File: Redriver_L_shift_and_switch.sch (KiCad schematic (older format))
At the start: 12 parts, among them U3 SN74AVCH16T245_DGV_48

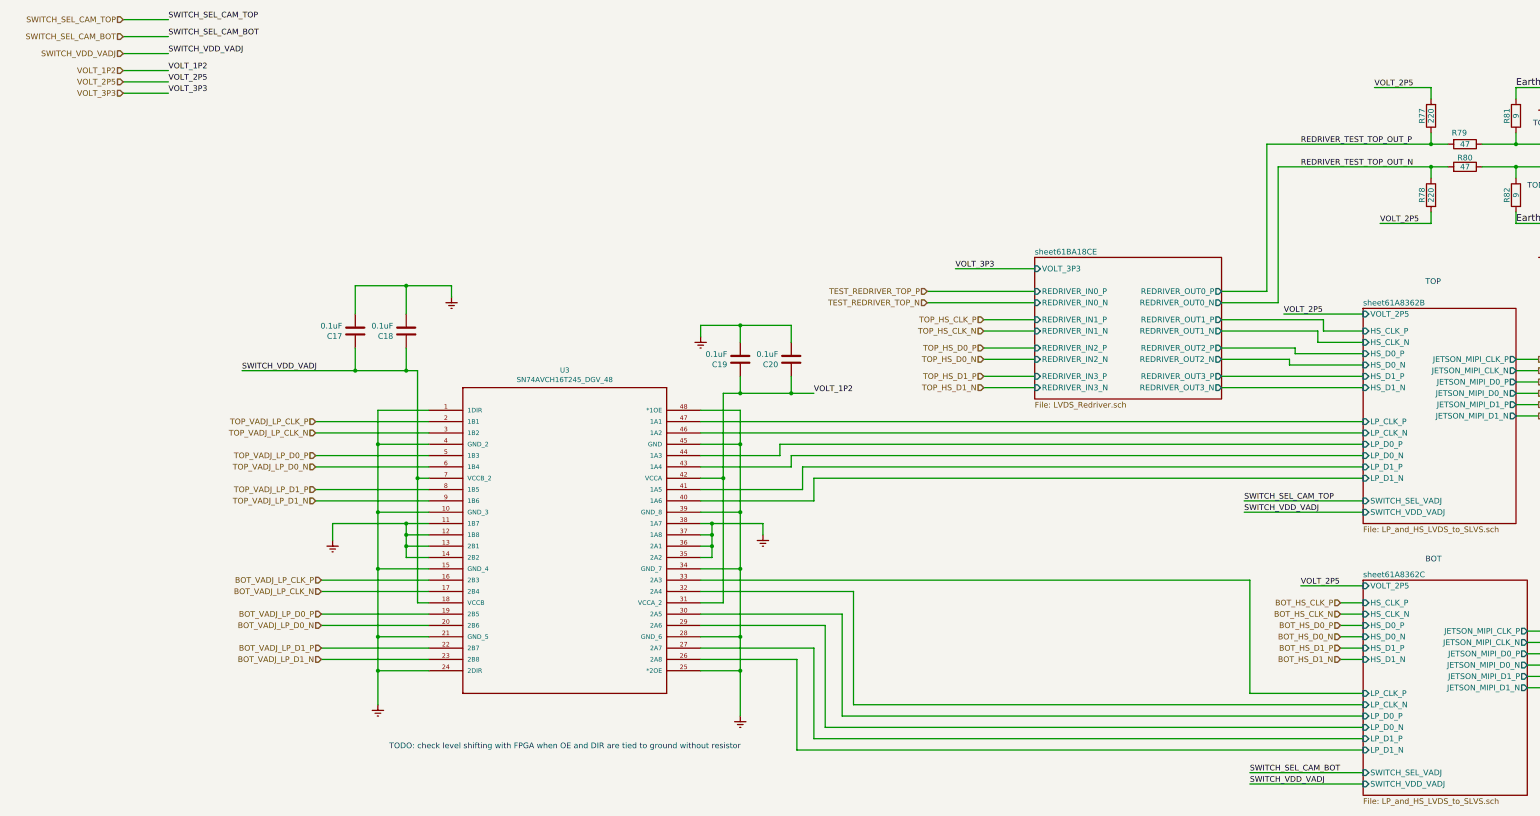
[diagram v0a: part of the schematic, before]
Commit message: good, added re-driver
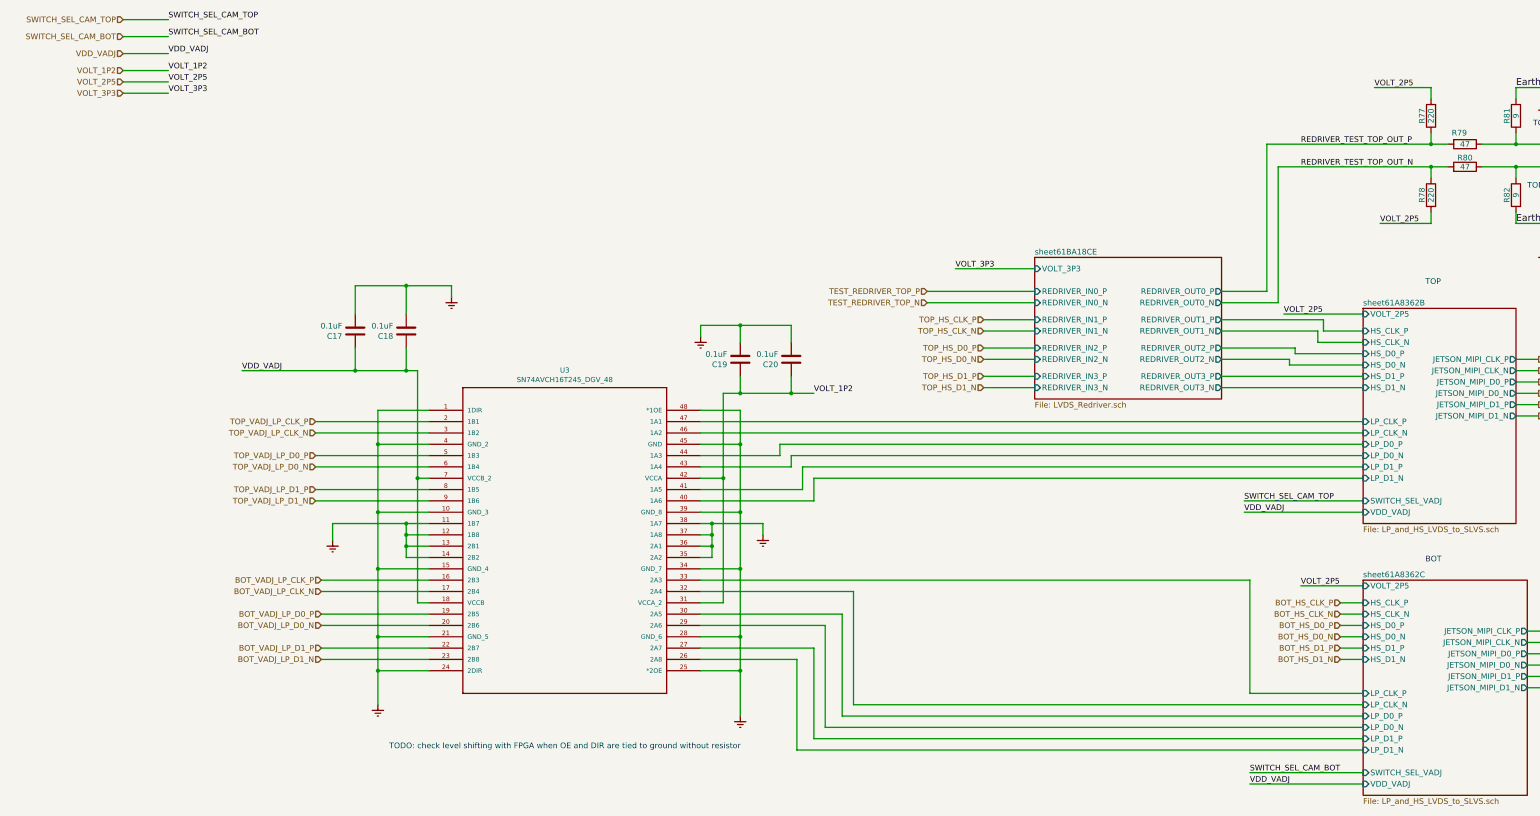
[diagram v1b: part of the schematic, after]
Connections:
- net SWITCH_VDD_VADJ renamed VDD_VADJ
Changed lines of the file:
@@
 $Descr A3 16535 11693
 encoding utf-8
-Sheet 23 32
+Sheet 11 20
 Title ""
 Date ""
@@
 F19 "LP_D0_N" I L 12550 7000 50
 F20 "SWITCH_SEL_VADJ" I L 12550 7400 50
-F21 "SWITCH_VDD_VADJ" I L 12550 7500 50
+F21 "VDD_VADJ" I L 12550 7500 50
 F22 "VOLT_2P5" I L 12550 5750 50
 $EndSheet
@@
 	12550 7500 11550 7500
 Text Label 11500 5100 0    50   ~ 0
-SWITCH_VDD_VADJ
+VDD_VADJ
 Text Label 11550 7500 0    50   ~ 0
-SWITCH_VDD_VADJ
+VDD_VADJ
 Text Label 11500 5000 0    50   ~ 0
 SWITCH_SEL_CAM_TOP
@@
 SWITCH_SEL_CAM_TOP
 Text HLabel 1600 1050 0    50   Input ~ 0
-SWITCH_VDD_VADJ
+VDD_VADJ
 Text HLabel 1600 900  0    50   Input ~ 0
 SWITCH_SEL_CAM_BOT
@@
 	1600 1050 2000 1050
 Text Label 2000 1050 0    50   ~ 0
-SWITCH_VDD_VADJ
+VDD_VADJ
 Text Label 2000 900  0    50   ~ 0
 SWITCH_SEL_CAM_BOT
@@
 Connection ~ 4200 4800
 Text Label 2650 3850 0    50   ~ 0
-SWITCH_VDD_VADJ
+VDD_VADJ
 $Comp
 L FMC_MIPI_v2:Earth #PWR?
@@
 F19 "LP_D0_N" I L 12550 4600 50
 F20 "SWITCH_SEL_VADJ" I L 12550 5000 50
-F21 "SWITCH_VDD_VADJ" I L 12550 5100 50
+F21 "VDD_VADJ" I L 12550 5100 50
 F22 "VOLT_2P5" I L 12550 3350 50
 $EndSheet
